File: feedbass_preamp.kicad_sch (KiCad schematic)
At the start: 12 parts, among them J1 Conn_01x04, U7 Opamp_Dual

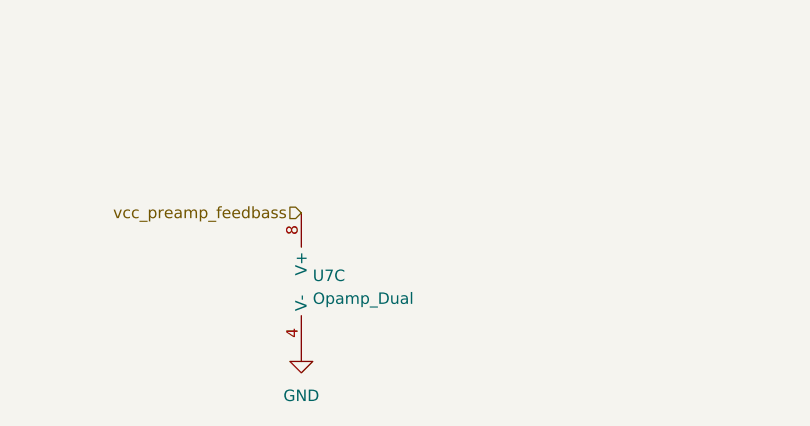
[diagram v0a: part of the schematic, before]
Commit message: add bypass caps to opamps + swap poweramps + layout progress
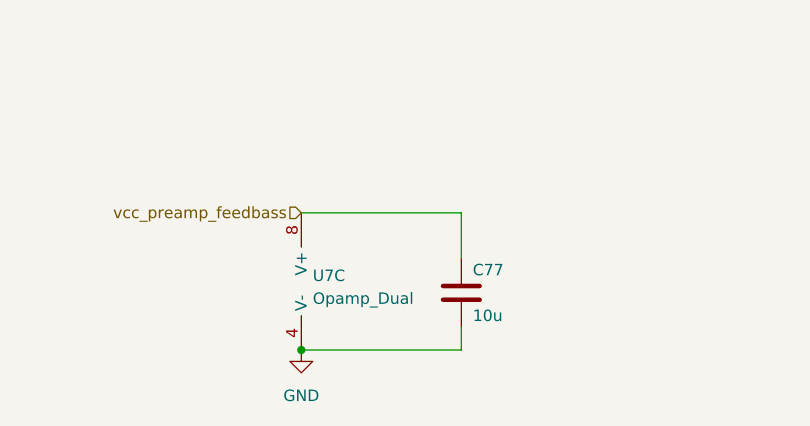
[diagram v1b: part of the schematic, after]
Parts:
- added C77: 10u, invendelirium_audio:C_0603, symbol Device:C
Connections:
- net GND: now also C77.2
- net vcc_preamp_feedbass: now also C77.1
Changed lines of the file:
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@@
   (junction (at 104.14 54.61) (diameter 0) (color 0 0 0 0)
+  )
+  (junction (at 134.62 125.73) (diameter 0) (color 0 0 0 0)
   )
   (junction (at 104.14 58.42) (diameter 0) (color 0 0 0 0)
@@
     (stroke (width 0) (type default))
   )
+  (wire (pts (xy 134.62 110.49) (xy 152.4 110.49))
+    (stroke (width 0) (type default))
+  )
   (wire (pts (xy 156.21 74.93) (xy 156.21 66.04))
     (stroke (width 0) (type default))
@@
     (stroke (width 0) (type default))
   )
+  (wire (pts (xy 152.4 123.19) (xy 152.4 125.73))
+    (stroke (width 0) (type default))
+  )
   (wire (pts (xy 171.45 74.93) (xy 173.99 74.93))
     (stroke (width 0) (type default))
   )
+  (wire (pts (xy 152.4 125.73) (xy 134.62 125.73))
+    (stroke (width 0) (type default))
+  )
   (wire (pts (xy 171.45 82.55) (xy 171.45 74.93))
     (stroke (width 0) (type default))
@@
   )
   (wire (pts (xy 173.99 69.85) (xy 168.91 69.85))
+    (stroke (width 0) (type default))
+  )
+  (wire (pts (xy 152.4 115.57) (xy 152.4 110.49))
     (stroke (width 0) (type default))
   )
@@
         )
       )
+    )
+  )
+  (symbol (lib_id "Device:C") (at 152.4 119.38 0) (unit 1)
+    (in_bom yes) (on_board yes) (dnp no)
+    (property "Reference" "C77" (at 153.67 116.84 0)
+      (effects (font (size 1.27 1.27)) (justify left))
+    )
+    (property "Value" "10u" (at 153.67 121.92 0)
+      (effects (font (size 1.27 1.27)) (justify left))
+    )
+    (property "Footprint" "invendelirium_audio:C_0603" (at 153.3652 123.19 0)
+      (effects (font (size 1.27 1.27)) hide)
+    )
+    (property "Datasheet" "~" (at 152.4 119.38 0)
+      (effects (font (size 1.27 1.27)) hide)
+    )
+    (property "Voltage" "16V" (at 152.4 119.38 0)
+      (effects (font (size 1.27 1.27)) hide)
+    )
+    (pin "1")
+    (pin "2")
+    (instances
+      (project "uberamp1"
+        (path "/310059c1-d84b-43e2-9c9a-0e426c534a12/5156a0a1-195e-40e3-846d-487893ba8fa7"
+          (reference "C77") (unit 1)
+        )
+        (path "/310059c1-d84b-43e2-9c9a-0e426c534a12/f0f90934-0ffc-42c4-856c-3b886cd79d06"
+          (reference "C78") (unit 1)
+        )
+        (path "/310059c1-d84b-43e2-9c9a-0e426c534a12/605c496f-1ba6-4b8d-86f6-e928e6401a1d"
+          (reference "CU7") (unit 1)
+        )
+        (path "/310059c1-d84b-43e2-9c9a-0e426c534a12/fb6b8bc8-ff14-4d64-816d-20c0f51b1294"
+          (reference "CU8") (unit 1)
+        )
+      )

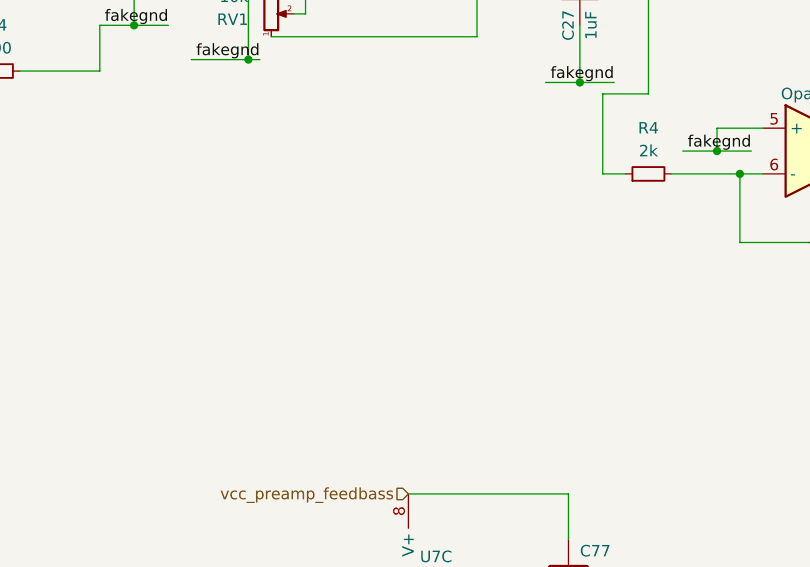
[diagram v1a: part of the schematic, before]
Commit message: add bypass caps to fakegnd
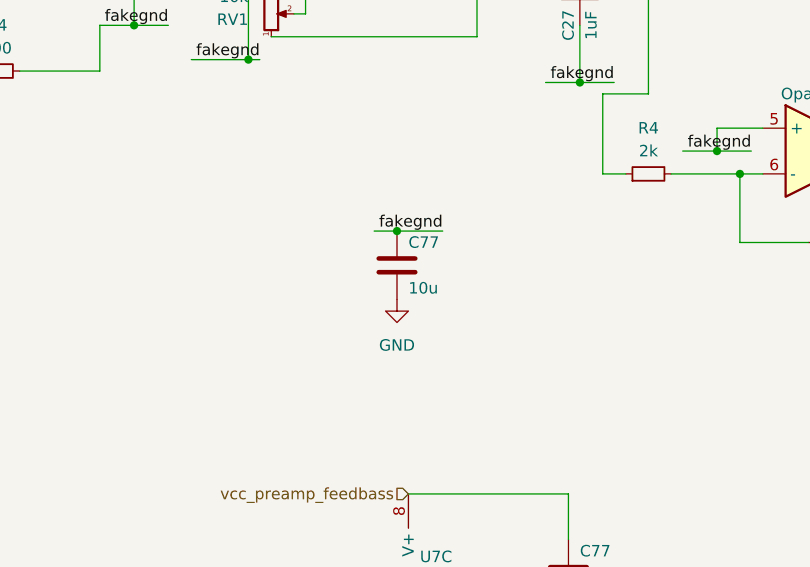
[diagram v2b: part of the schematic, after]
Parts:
- added C77: 10u, invendelirium_audio:C_0603, symbol Device:C
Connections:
- net GND: now also C77.2
- net fakegnd: now also C77.1
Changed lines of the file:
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@@
   (junction (at 104.14 58.42) (diameter 0) (color 0 0 0 0)
+  )
+  (junction (at 133.35 81.28) (diameter 0) (color 0 0 0 0)
   )
   (no_connect (at 64.77 57.15))
@@
     (stroke (width 0) (type default))
   )
+  (wire (pts (xy 133.35 81.28) (xy 138.43 81.28))
+    (stroke (width 0) (type default))
+  )
   (wire (pts (xy 104.14 58.42) (xy 107.95 58.42))
     (stroke (width 0) (type default))
@@
   )
   (wire (pts (xy 142.24 49.53) (xy 140.97 49.53))
+    (stroke (width 0) (type default))
+  )
+  (wire (pts (xy 130.81 81.28) (xy 133.35 81.28))
     (stroke (width 0) (type default))
   )
@@
   )
   (label "fakegnd" (at 208.28 85.09 180) (fields_autoplaced)
+    (effects (font (size 1.27 1.27)) (justify right bottom))
+  )
+  (label "fakegnd" (at 138.43 81.28 180) (fields_autoplaced)
     (effects (font (size 1.27 1.27)) (justify right bottom))
   )
@@
         (path "/310059c1-d84b-43e2-9c9a-0e426c534a12/fb6b8bc8-ff14-4d64-816d-20c0f51b1294"
           (reference "C73") (unit 1)
+        )
+      )
+    )
+  )
+  (symbol (lib_id "Device:C") (at 133.35 85.09 0) (unit 1)
+    (in_bom yes) (on_board yes) (dnp no)
+    (property "Reference" "C77" (at 134.62 82.55 0)
+      (effects (font (size 1.27 1.27)) (justify left))
+    )
+    (property "Value" "10u" (at 134.62 87.63 0)
+      (effects (font (size 1.27 1.27)) (justify left))
+    )
+    (property "Footprint" "invendelirium_audio:C_0603" (at 134.3152 88.9 0)
+      (effects (font (size 1.27 1.27)) hide)
+    )
+    (property "Datasheet" "~" (at 133.35 85.09 0)
+      (effects (font (size 1.27 1.27)) hide)
+    )
+    (property "Voltage" "16V" (at 133.35 85.09 0)
+      (effects (font (size 1.27 1.27)) hide)
+    )
+    (pin "1")
+    (pin "2")
+    (instances
+      (project "uberamp1"
+        (path "/310059c1-d84b-43e2-9c9a-0e426c534a12/5156a0a1-195e-40e3-846d-487893ba8fa7"
+          (reference "C77") (unit 1)
+        )
+        (path "/310059c1-d84b-43e2-9c9a-0e426c534a12/f0f90934-0ffc-42c4-856c-3b886cd79d06"
+          (reference "C78") (unit 1)
+        )
+        (path "/310059c1-d84b-43e2-9c9a-0e426c534a12/c6ef957f-dbb4-496d-aec2-44492c2243c4"
+          (reference "C77") (unit 1)
+        )
+        (path "/310059c1-d84b-43e2-9c9a-0e426c534a12/1727f815-1282-4ad8-874c-d1f66f4d7fbe"
+          (reference "C78") (unit 1)
+        )
+        (path "/310059c1-d84b-43e2-9c9a-0e426c534a12/e09aca01-5377-42b6-85e8-8afbf1155690"
+          (reference "C79") (unit 1)
+        )
+        (path "/310059c1-d84b-43e2-9c9a-0e426c534a12/b23c2595-3b45-43cf-b3fd-b0c94e6d7f84"
+          (reference "C80") (unit 1)
+        )
+        (path "/310059c1-d84b-43e2-9c9a-0e426c534a12/605c496f-1ba6-4b8d-86f6-e928e6401a1d"
+          (reference "CRB0") (unit 1)
+        )
+        (path "/310059c1-d84b-43e2-9c9a-0e426c534a12/fb6b8bc8-ff14-4d64-816d-20c0f51b1294"
+          (reference "CRB1") (unit 1)
         )
       )
@@
         )
       )
+    )
+  )
+  (symbol (lib_id "power:GND") (at 133.35 88.9 0) (unit 1)
+    (in_bom yes) (on_board yes) (dnp no) (fields_autoplaced)
+    (property "Reference" "#PWR02" (at 133.35 95.25 0)
+      (effects (font (size 1.27 1.27)) hide)
+    )
+    (property "Value" "GND" (at 133.35 93.98 0)
+      (effects (font (size 1.27 1.27)))
+    )
+    (property "Footprint" "" (at 133.35 88.9 0)
+      (effects (font (size 1.27 1.27)) hide)
+    )
+    (property "Datasheet" "" (at 133.35 88.9 0)
+      (effects (font (size 1.27 1.27)) hide)
+    )
+    (pin "1")
+    (instances
+      (project "uberamp1"
+        (path "/310059c1-d84b-43e2-9c9a-0e426c534a12/c6ef957f-dbb4-496d-aec2-44492c2243c4"
+          (reference "#PWR02") (unit 1)
+        )
+        (path "/310059c1-d84b-43e2-9c9a-0e426c534a12/605c496f-1ba6-4b8d-86f6-e928e6401a1d"
+          (reference "#PWR082") (unit 1)
+        )
+        (path "/310059c1-d84b-43e2-9c9a-0e426c534a12/fb6b8bc8-ff14-4d64-816d-20c0f51b1294"
+          (reference "#PWR083") (unit 1)
+        )
+      )

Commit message: update feedbass components
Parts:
- C27: value 1uF -> 0.33uF; footprint invendelirium_audio:CB052D0105KBC film cap -> Capacitor_SMD:C_1206_3216Metric; PartNumber CB052D0105KBC -> (none)
- RV1: value 10k -> 1k; footprint Potentiometer_SMD:Potentiometer_Bourns_TC33X_Vertical -> invendelirium_audio:PV37X
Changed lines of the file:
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@@
       (effects (font (size 1.27 1.27)))
     )
-    (property "Value" "1uF" (at 154.94 58.42 90)
-      (effects (font (size 1.27 1.27)))
-    )
-    (property "Footprint" "invendelirium_audio:CB052D0105KBC film cap" (at 154.6352 58.42 0)
+    (property "Value" "0.33uF" (at 154.94 58.42 90)
+      (effects (font (size 1.27 1.27)))
+    )
+    (property "Footprint" "Capacitor_SMD:C_1206_3216Metric" (at 154.6352 58.42 0)
       (effects (font (size 1.27 1.27)) hide)
     )
@@
       (effects (font (size 1.27 1.27)) hide)
     )
-    (property "PartNumber" "CB052D0105KBC" (at 153.67 54.61 90)
+    (property "PartNumber" "" (at 153.67 54.61 90)
       (effects (font (size 1.27 1.27)) hide)
     )
@@
       (effects (font (size 1.27 1.27)) (justify right))
     )
-    (property "Value" "10k" (at 116.84 55.245 0)
+    (property "Value" "1k" (at 116.84 55.245 0)
       (effects (font (size 1.27 1.27)) (justify right))
     )
-    (property "Footprint" "Potentiometer_SMD:Potentiometer_Bourns_TC33X_Vertical" (at 119.38 57.15 0)
-      (effects (font (size 1.27 1.27)) hide)
-    )
+    (property "Footprint" "invendelirium_audio:PV37X" (at 119.38 57.15 0)
+      (effects (font (size 1.27 1.27)) hide)
+    )

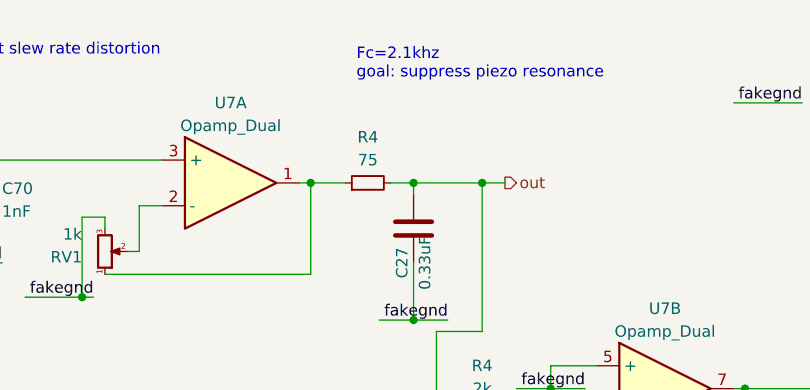
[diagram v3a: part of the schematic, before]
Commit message: fix feedbass filter
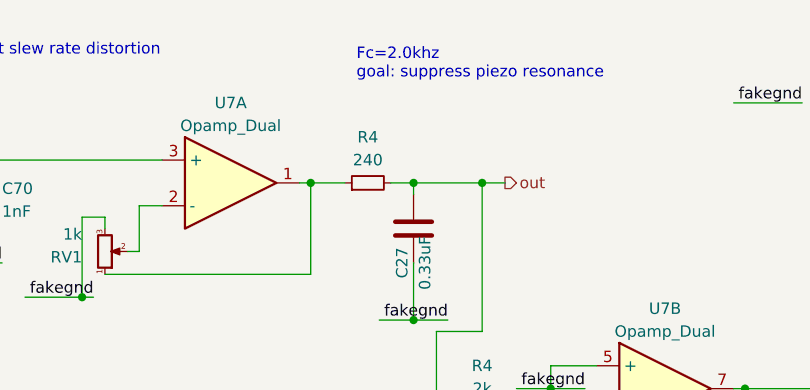
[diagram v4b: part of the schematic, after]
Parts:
- R4: value 75 -> 240
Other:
- note added: "Fc=2.0khz goal: suppress piezo resonance"
- note removed: "Fc=2.1khz goal: suppress piezo resonance"
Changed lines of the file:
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@@
     (effects (font (size 1.27 1.27)) (justify left bottom))
   )
-  (text "Fc=2.1khz\ngoal: suppress piezo resonance" (at 147.32 38.1 0)
+  (text "Fc=2.0khz\ngoal: suppress piezo resonance" (at 147.32 38.1 0)
     (effects (font (size 1.27 1.27)) (justify left bottom))
   )
@@
       (effects (font (size 1.27 1.27)))
     )
-    (property "Value" "75" (at 148.59 46.99 90)
+    (property "Value" "240" (at 148.59 46.99 90)
       (effects (font (size 1.27 1.27)))
     )

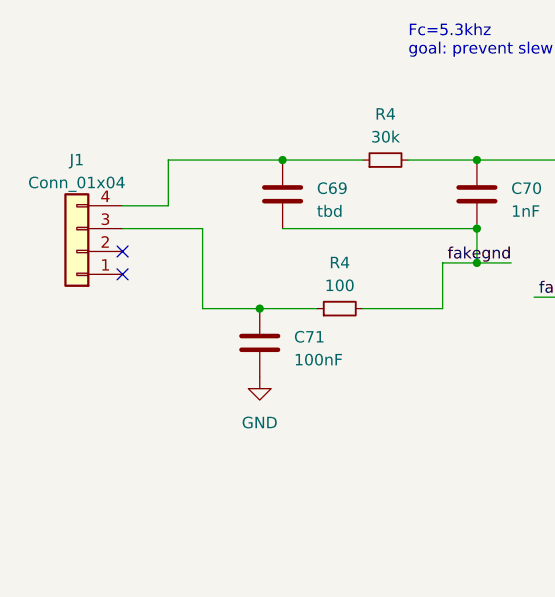
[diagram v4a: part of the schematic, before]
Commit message: add dsp and esp32... schematic mostly done
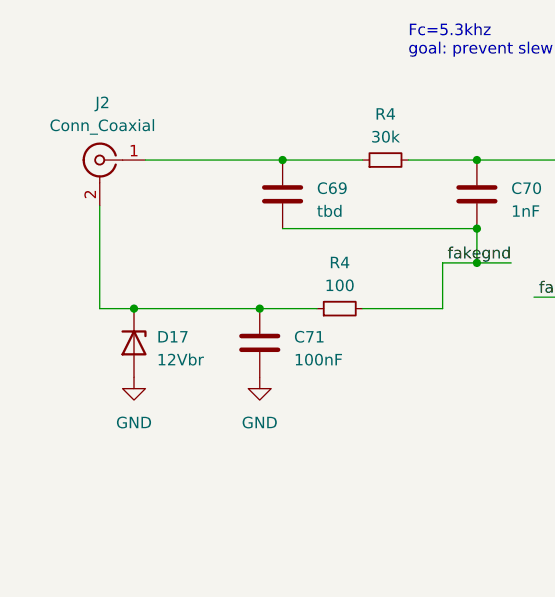
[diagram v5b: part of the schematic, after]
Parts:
- removed J1: Conn_01x04, Connector_JST:JST_EH_S4B-EH_1x04_P2.50mm_Horizontal, symbol Connector_Generic:Conn_01x04
- added D17: 12Vbr, Diode_SMD:D_SOD-323_HandSoldering, symbol Device:D_Zener
- added J2: Conn_Coaxial, invendelirium_audio:mmcx_f_vert, symbol Connector:Conn_Coaxial
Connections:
- net GND: now also D17.2 (A)
- net at C69.1, R4.1: now also J2.1 (In)
- net at C71.1, R4.1: now also D17.1 (K), J2.2 (Ext)
- no-connect marks 2 -> 0
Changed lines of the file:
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@@
   (junction (at 142.24 49.53) (diameter 0) (color 0 0 0 0)
   )
+  (junction (at 66.04 63.5) (diameter 0) (color 0 0 0 0)
+  )
   (junction (at 204.47 85.09) (diameter 0) (color 0 0 0 0)
   )
@@
   (junction (at 133.35 81.28) (diameter 0) (color 0 0 0 0)
   )
-  (no_connect (at 64.77 57.15))
-  (no_connect (at 64.77 59.69))
   (wire (pts (xy 121.92 57.15) (xy 123.19 57.15))
     (stroke (width 0) (type default))
@@
     (stroke (width 0) (type default))
   )
-  (wire (pts (xy 73.66 63.5) (xy 80.01 63.5))
+  (wire (pts (xy 62.23 63.5) (xy 66.04 63.5))
+    (stroke (width 0) (type default))
+  )
+  (wire (pts (xy 66.04 63.5) (xy 80.01 63.5))
     (stroke (width 0) (type default))
   )
@@
     (stroke (width 0) (type default))
   )
-  (wire (pts (xy 73.66 54.61) (xy 73.66 63.5))
+  (wire (pts (xy 62.23 52.07) (xy 62.23 63.5))
     (stroke (width 0) (type default))
   )
@@
     (stroke (width 0) (type default))
   )
-  (wire (pts (xy 69.85 46.99) (xy 82.55 46.99))
+  (wire (pts (xy 67.31 46.99) (xy 82.55 46.99))
     (stroke (width 0) (type default))
   )
@@
     (stroke (width 0) (type default))
   )
-  (wire (pts (xy 64.77 54.61) (xy 73.66 54.61))
-    (stroke (width 0) (type default))
-  )
   (wire (pts (xy 190.5 72.39) (xy 207.01 72.39))
     (stroke (width 0) (type default))
@@
   )
   (wire (pts (xy 123.19 52.07) (xy 125.73 52.07))
-    (stroke (width 0) (type default))
-  )
-  (wire (pts (xy 64.77 52.07) (xy 69.85 52.07))
-    (stroke (width 0) (type default))
-  )
-  (wire (pts (xy 69.85 52.07) (xy 69.85 46.99))
     (stroke (width 0) (type default))
   )
@@
     )
   )
+  (symbol (lib_id "power:GND") (at 66.04 71.12 0) (unit 1)
+    (in_bom yes) (on_board yes) (dnp no) (fields_autoplaced)
+    (property "Reference" "#PWR02" (at 66.04 77.47 0)
+      (effects (font (size 1.27 1.27)) hide)
+    )
+    (property "Value" "GND" (at 66.04 76.2 0)
+      (effects (font (size 1.27 1.27)))
+    )
+    (property "Footprint" "" (at 66.04 71.12 0)
+      (effects (font (size 1.27 1.27)) hide)
+    )
+    (property "Datasheet" "" (at 66.04 71.12 0)
+      (effects (font (size 1.27 1.27)) hide)
+    )
+    (pin "1")
+    (instances
+      (project "uberamp1"
+        (path "/310059c1-d84b-43e2-9c9a-0e426c534a12/c6ef957f-dbb4-496d-aec2-44492c2243c4"
+          (reference "#PWR02") (unit 1)
+        )
+        (path "/310059c1-d84b-43e2-9c9a-0e426c534a12/605c496f-1ba6-4b8d-86f6-e928e6401a1d"
+          (reference "#PWR0149") (unit 1)
+        )
+        (path "/310059c1-d84b-43e2-9c9a-0e426c534a12/fb6b8bc8-ff14-4d64-816d-20c0f51b1294"
+          (reference "#PWR0150") (unit 1)
+        )
+      )
+    )
+  )
   (symbol (lib_id "Device:C") (at 104.14 50.8 0) (unit 1)
     (in_bom yes) (on_board yes) (dnp no) (fields_autoplaced)
@@
         (path "/310059c1-d84b-43e2-9c9a-0e426c534a12/fb6b8bc8-ff14-4d64-816d-20c0f51b1294"
           (reference "CRB1") (unit 1)
-        )
-      )
-    )
-  )
-  (symbol (lib_id "Connector_Generic:Conn_01x04") (at 59.69 57.15 180) (unit 1)
-    (in_bom yes) (on_board yes) (dnp no) (fields_autoplaced)
-    (property "Reference" "J1" (at 59.69 46.99 0)
-      (effects (font (size 1.27 1.27)))
-    )
-    (property "Value" "Conn_01x04" (at 59.69 49.53 0)
-      (effects (font (size 1.27 1.27)))
-    )
-    (property "Footprint" "Connector_JST:JST_EH_S4B-EH_1x04_P2.50mm_Horizontal" (at 59.69 57.15 0)
-      (effects (font (size 1.27 1.27)) hide)
-    )
-    (property "Datasheet" "~" (at 59.69 57.15 0)
-      (effects (font (size 1.27 1.27)) hide)
-    )
-    (pin "1")
-    (pin "2")
-    (pin "3")
-    (pin "4")
-    (instances
-      (project "uberamp1"
-        (path "/310059c1-d84b-43e2-9c9a-0e426c534a12/605c496f-1ba6-4b8d-86f6-e928e6401a1d"
-          (reference "J1") (unit 1)
-        )
-        (path "/310059c1-d84b-43e2-9c9a-0e426c534a12/fb6b8bc8-ff14-4d64-816d-20c0f51b1294"
-          (reference "J2") (unit 1)
         )
       )
@@
     )
   )
+  (symbol (lib_id "Connector:Conn_Coaxial") (at 62.23 46.99 0) (mirror y) (unit 1)
+    (in_bom yes) (on_board yes) (dnp no) (fields_autoplaced)
+    (property "Reference" "J2" (at 62.5474 40.64 0)
+      (effects (font (size 1.27 1.27)))
+    )
+    (property "Value" "Conn_Coaxial" (at 62.5474 43.18 0)
+      (effects (font (size 1.27 1.27)))
+    )
+    (property "Footprint" "invendelirium_audio:mmcx_f_vert" (at 62.23 46.99 0)
+      (effects (font (size 1.27 1.27)) hide)
+    )
+    (property "Datasheet" " ~" (at 62.23 46.99 0)
+      (effects (font (size 1.27 1.27)) hide)
+    )
+    (pin "1")
+    (pin "2")
+    (instances
+      (project "uberamp1"
+        (path "/310059c1-d84b-43e2-9c9a-0e426c534a12/605c496f-1ba6-4b8d-86f6-e928e6401a1d"
+          (reference "J2") (unit 1)
+        )
+        (path "/310059c1-d84b-43e2-9c9a-0e426c534a12/fb6b8bc8-ff14-4d64-816d-20c0f51b1294"
+          (reference "J?") (unit 1)
+        )
+      )
+    )
+  )
   (symbol (lib_id "Device:Opamp_Dual") (at 133.35 49.53 0) (unit 1)
     (in_bom yes) (on_board yes) (dnp no) (fields_autoplaced)
@@
         )
       )
+    )
+  )
+  (symbol (lib_id "Device:D_Zener") (at 66.04 67.31 270) (unit 1)
+    (in_bom yes) (on_board yes) (dnp no) (fields_autoplaced)
+    (property "Reference" "D17" (at 68.58 66.675 90)
+      (effects (font (size 1.27 1.27)) (justify left))
+    )
+    (property "Value" "12Vbr" (at 68.58 69.215 90)
+      (effects (font (size 1.27 1.27)) (justify left))
+    )
+    (property "Footprint" "Diode_SMD:D_SOD-323_HandSoldering" (at 66.04 67.31 0)
+      (effects (font (size 1.27 1.27)) hide)
+    )
+    (property "Datasheet" "~" (at 66.04 67.31 0)
+      (effects (font (size 1.27 1.27)) hide)
+    )
+    (property "PN" "P1CH7.0A-AU_R1_000A1" (at 66.04 67.31 90)
+      (effects (font (size 1.016 1.016)) hide)
+    )
+    (pin "1")
+    (pin "2")
+    (instances
+      (project "uberamp1"
+        (path "/310059c1-d84b-43e2-9c9a-0e426c534a12/605c496f-1ba6-4b8d-86f6-e928e6401a1d"
+          (reference "D17") (unit 1)
+        )
+        (path "/310059c1-d84b-43e2-9c9a-0e426c534a12/fb6b8bc8-ff14-4d64-816d-20c0f51b1294"
+          (reference "D?") (unit 1)
+        )
+      )
